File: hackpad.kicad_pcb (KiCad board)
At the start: 2 copper layers, 83.3 x 101.1 mm, 33 parts, among them SW1 SW_Push, SW10 SW_Push, SW11 SW_Push, SW12 SW_Push, SW13 SW_Push, SW14 SW_Push, SW15 SW_Push, SW16 SW_Push, SW2 SW_Push, SW3 SW_Push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

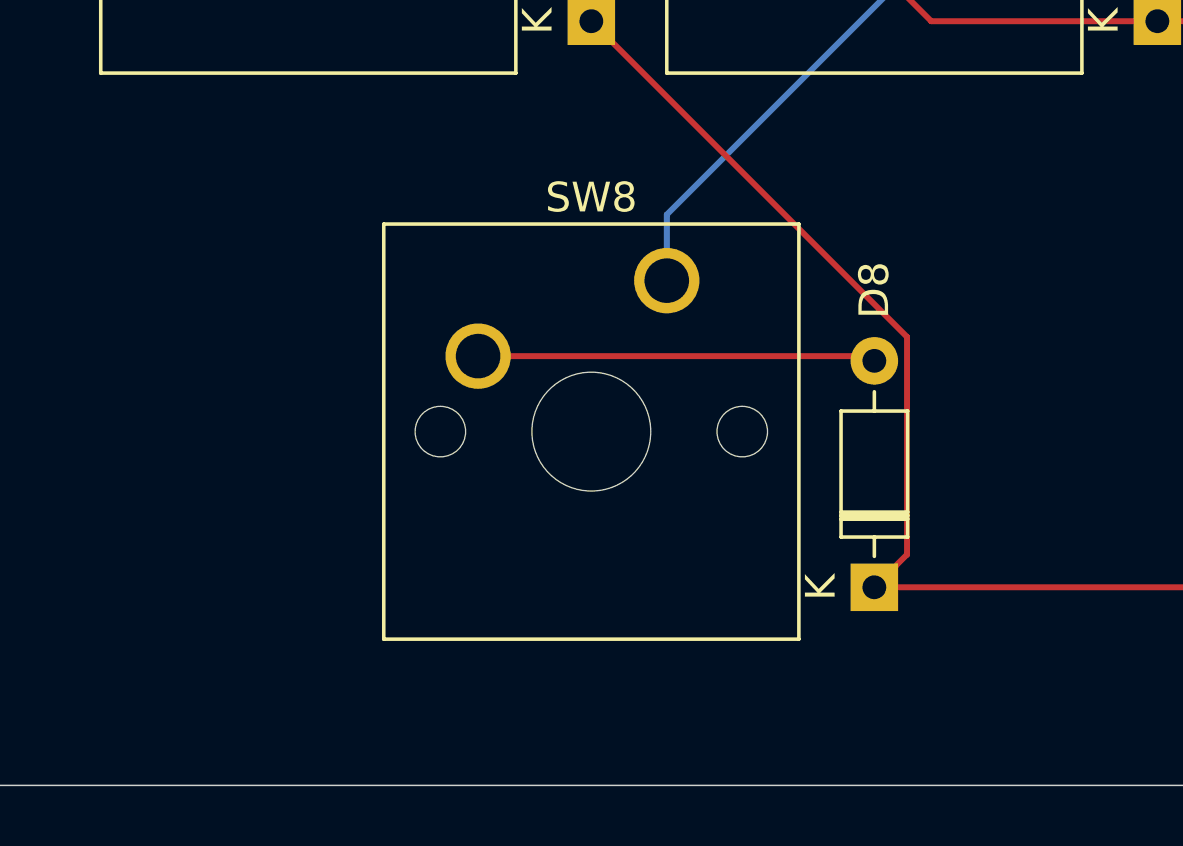
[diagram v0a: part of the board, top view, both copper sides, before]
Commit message: Updated switch 8 to 2u size
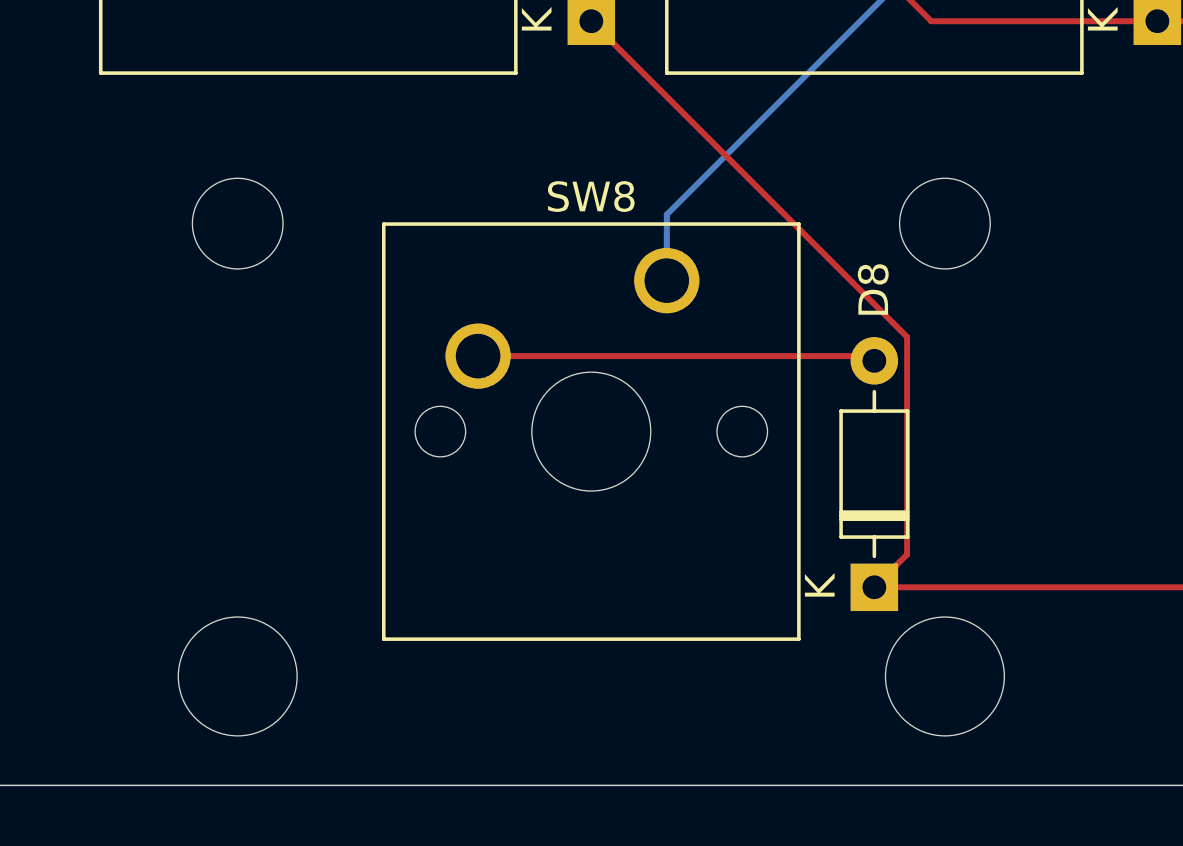
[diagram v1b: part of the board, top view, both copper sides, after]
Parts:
- SW8: footprint Button_Switch_Keyboard:SW_Cherry_MX_1.00u_PCB -> Button_Switch_Keyboard:SW_Cherry_MX_2.00u_PCB
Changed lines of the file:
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@@
 		)
 	)
-	(footprint "Button_Switch_Keyboard:SW_Cherry_MX_1.00u_PCB"
+	(footprint "Button_Switch_Keyboard:SW_Cherry_MX_2.00u_PCB"
 		(layer "F.Cu")
 		(at 50.165 116.36375)
-		(descr "Cherry MX keyswitch, 1.00u, PCB mount, http://cherryamericas.com/wp-content/uploads/2014/12/mx_cat.pdf")
-		(tags "Cherry MX keyswitch 1.00u PCB")
+		(descr "Cherry MX keyswitch, 2.00u, PCB mount, http://cherryamericas.com/wp-content/uploads/2014/12/mx_cat.pdf")
+		(tags "Cherry MX keyswitch 2.00u PCB")
 		(property "Reference" "SW8"
 			(at -2.54 -2.794 0)
@@
 			)
 		)
-		(property "Footprint" "Button_Switch_Keyboard:SW_Cherry_MX_1.00u_PCB"
+		(property "Footprint" "Button_Switch_Keyboard:SW_Cherry_MX_2.00u_PCB"
 			(at 0 0 0)
 			(unlocked yes)
@@
 		)
 		(fp_line
-			(start -12.065 -4.445)
-			(end 6.985 -4.445)
-			(stroke
-				(width 0.15)
-				(type solid)
-			)
-			(layer "Dwgs.User")
-		)
-		(fp_line
-			(start -12.065 14.605)
-			(end -12.065 -4.445)
-			(stroke
-				(width 0.15)
-				(type solid)
-			)
-			(layer "Dwgs.User")
-		)
-		(fp_line
-			(start 6.985 -4.445)
-			(end 6.985 14.605)
-			(stroke
-				(width 0.15)
-				(type solid)
-			)
-			(layer "Dwgs.User")
-		)
-		(fp_line
-			(start 6.985 14.605)
-			(end -12.065 14.605)
+			(start -21.59 -4.445)
+			(end 16.51 -4.445)
+			(stroke
+				(width 0.15)
+				(type solid)
+			)
+			(layer "Dwgs.User")
+		)
+		(fp_line
+			(start -21.59 14.605)
+			(end -21.59 -4.445)
+			(stroke
+				(width 0.15)
+				(type solid)
+			)
+			(layer "Dwgs.User")
+		)
+		(fp_line
+			(start 16.51 -4.445)
+			(end 16.51 14.605)
+			(stroke
+				(width 0.15)
+				(type solid)
+			)
+			(layer "Dwgs.User")
+		)
+		(fp_line
+			(start 16.51 14.605)
+			(end -21.59 14.605)
 			(stroke
 				(width 0.15)
@@
 				)
 			)
+		)
+		(pad "" np_thru_hole circle
+			(at -14.44 -1.92)
+			(size 3.05 3.05)
+			(drill 3.05)
+			(layers "*.Cu" "*.Mask")
+		)
+		(pad "" np_thru_hole circle
+			(at -14.44 13.32)
+			(size 4 4)
+			(drill 4)
+			(layers "*.Cu" "*.Mask")
 		)
 		(pad "" np_thru_hole circle
@@
 			(size 1.7 1.7)
 			(drill 1.7)
+			(layers "*.Cu" "*.Mask")
+		)
+		(pad "" np_thru_hole circle
+			(at 9.36 -1.92)
+			(size 3.05 3.05)
+			(drill 3.05)
+			(layers "*.Cu" "*.Mask")
+		)
+		(pad "" np_thru_hole circle
+			(at 9.36 13.32)
+			(size 4 4)
+			(drill 4)
 			(layers "*.Cu" "*.Mask")
 		)
@@
 			(pintype "passive")
 		)
-		(model "${KICAD8_3DMODEL_DIR}/Button_Switch_Keyboard.3dshapes/SW_Cherry_MX_1.00u_PCB.wrl"
+		(model "${KICAD8_3DMODEL_DIR}/Button_Switch_Keyboard.3dshapes/SW_Cherry_MX_2.00u_PCB.wrl"
 			(offset
 				(xyz 0 0 0)

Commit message: Added silkscreen art
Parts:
- added G***: LOGO, LOGO, B.Cu at (64.3, 92.2)
- added G***: LOGO, LOGO, B.Cu at (69.7, 45.0)
